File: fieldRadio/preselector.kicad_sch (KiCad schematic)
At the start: 48 parts, among them K1 G5V-2, K2 G5V-2, K3 G5V-2, K4 G5V-2, Q1 MMBT3904, Q2 MMBT3904, Q3 MMBT3904, Q4 MMBT3904, Q5 MMBT3904

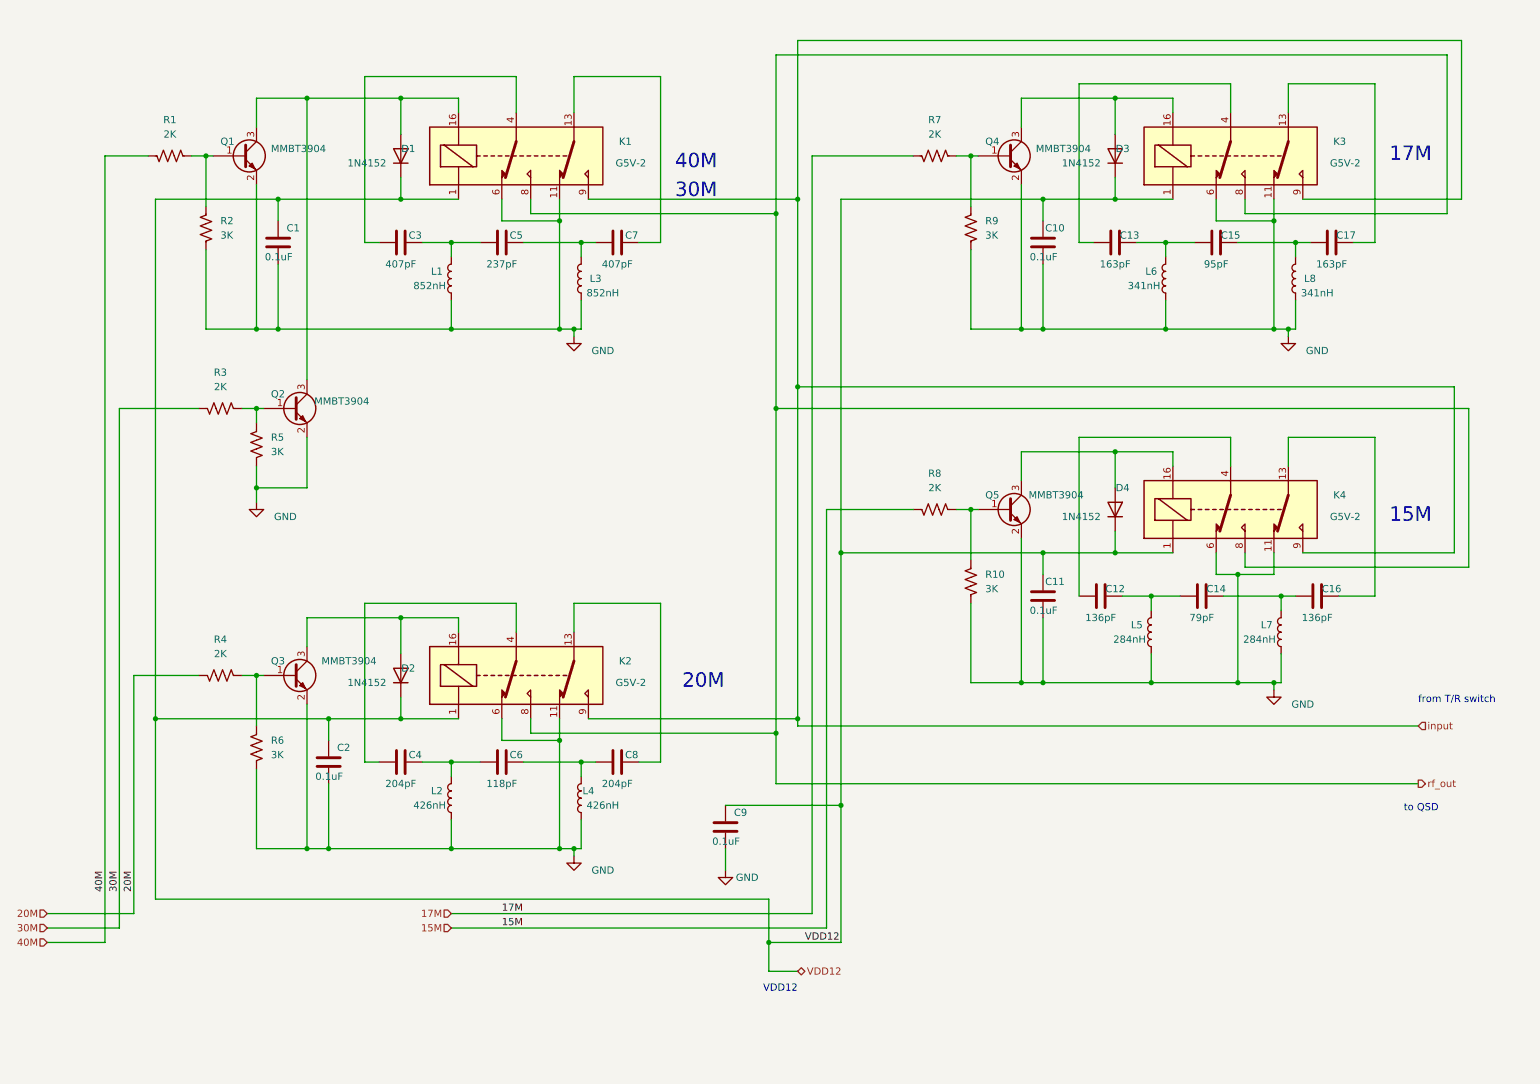
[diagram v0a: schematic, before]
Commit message: Building fieldradio schematic
in process of building field radio schematics
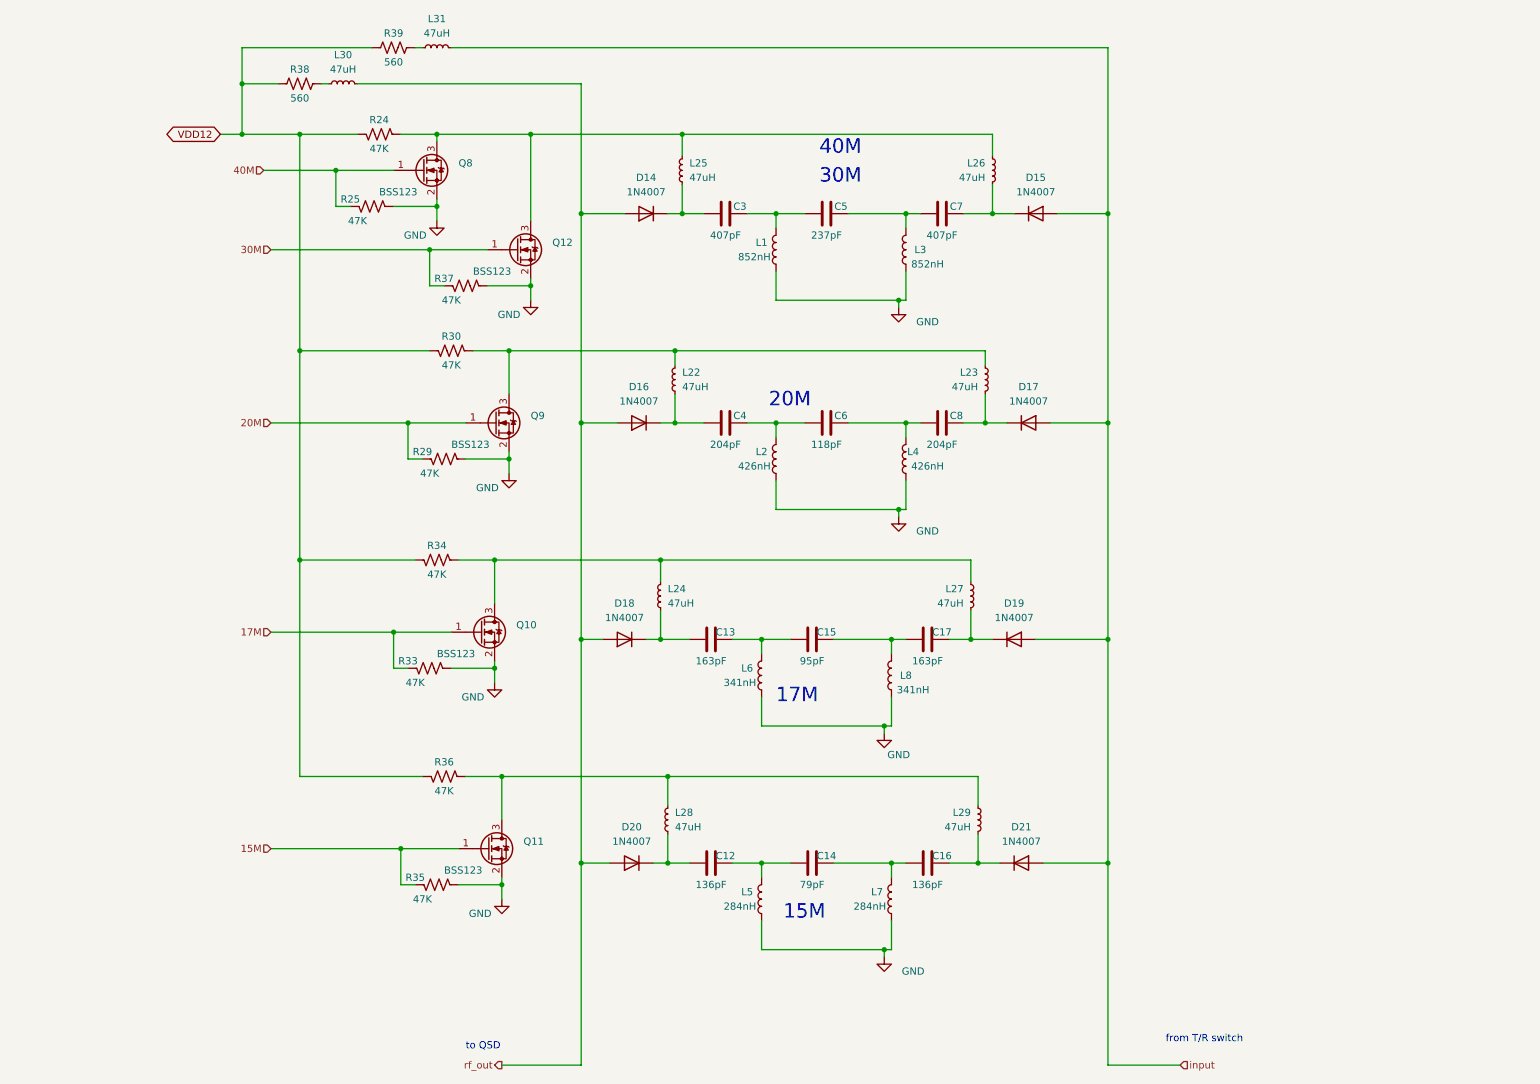
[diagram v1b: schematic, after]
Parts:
- removed C1, C10, C11, C2, C9: 0.1uF, Capacitor_SMD:C_0603_1608Metric_Pad1.08x0.95mm_HandSolder, symbol Device:C
- removed D1, D2, D3, D4: 1N4152, Diode_THT:D_DO-41_SOD81_P7.62mm_Horizontal, symbol Device:D
- removed K1, K2, K3, K4: G5V-2, Relay_THT:Relay_DPDT_Omron_G5V-2, symbol Relay:G5V-2
- removed Q1, Q2, Q3, Q4, Q5: MMBT3904, Package_TO_SOT_SMD:SOT-23, symbol Device:Q_NPN_BEC
- removed R1, R3, R4, R7, R8: 2K, Resistor_SMD:R_0603_1608Metric_Pad0.98x0.95mm_HandSolder, symbol Device:R_US
- removed R10, R2, R5, R6, R9: 3K, Resistor_SMD:R_0603_1608Metric_Pad0.98x0.95mm_HandSolder, symbol Device:R_US
- added D14, D15, D16, D17, D18, D19, D20, D21: 1N4007, Diode_THT:D_DO-41_SOD81_P10.16mm_Horizontal, symbol Diode:1N4007
- added L22, L23, L24, L25, L26, L27, L28, L29, L30, L31: 47uH, Inductor_THT:L_Axial_L11.0mm_D4.5mm_P7.62mm_Vertical_Fastron_MECC, symbol Device:L_Small
- added Q10, Q11, Q12, Q8, Q9: BSS123, Package_TO_SOT_SMD:SOT-23-3, symbol Device:Q_NMOS_GSD
- added R24, R25, R29, R30, R33, R34, R35, R36, R37: 47K, Resistor_SMD:R_0603_1608Metric_Pad0.98x0.95mm_HandSolder, symbol Device:R_US
- added R38, R39: 560, Resistor_THT:R_Axial_DIN0617_L17.0mm_D6.0mm_P20.32mm_Horizontal, symbol Device:R_US
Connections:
- net 15M: now also Q11.1 (G), R35.2
- net 17M: now also Q10.1 (G), R33.2
- net 20M: now also Q9.1 (G), R29.2
- net 30M: now also Q12.1 (G), R37.2
- net 40M: now also Q8.1 (G), R25.2
- net GND: now also Q10.2 (S), Q11.2 (S), Q12.2 (S), Q8.2 (S), Q9.2 (S), R25.1, R29.1, R33.1, R35.1, R37.1
- net VDD12: now also R24.2, R30.2, R34.2, R36.2, R38.1, R39.1
- net input: now also D15.2 (A), D17.2 (A), D19.2 (A), D21.2 (A), L31.2
- net rf_out: now also D14.2 (A), D16.2 (A), D18.2 (A), D20.2 (A), L30.2
- net at C8.1: now also D17.1 (K), L23.1
- net at C4.2: now also D16.1 (K), L22.1
- net at C16.1: now also D21.1 (K), L29.1
- net at C12.2: now also D20.1 (K), L28.1
- net at C17.1: now also D19.1 (K), L27.1
- net at C13.2: now also D18.1 (K), L24.1
- net at C7.1: now also D15.1 (K), L26.1
- net at C3.2: now also D14.1 (K), L25.1
- new net: L31.1, R39.2
- new net: L28.2, L29.2, Q11.3 (D), R36.1
- new net: L24.2, L27.2, Q10.3 (D), R34.1
- new net: L22.2, L23.2, Q9.3 (D), R30.1
- new net: L25.2, L26.2, Q12.3 (D), Q8.3 (D), R24.1
- new net: L30.1, R38.2
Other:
- note removed: "VDD12"
- moved on the sheet: C12, C13, C14, C15, C16, C17, C3, C4, C5, C6, C7, C8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

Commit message: More schematic dev.
More schematic development
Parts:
- removed C5: 237pF, Capacitor_SMD:C_0805_2012Metric_Pad1.18x1.45mm_HandSolder, symbol Device:C
- removed L1: 852nH, Inductor_THT:L_Toroid_Vertical_L13.0mm_W6.5mm_P5.60mm, symbol Device:L
- added C91: 237pF, Capacitor_SMD:C_0805_2012Metric_Pad1.18x1.45mm_HandSolder, symbol Device:C
- added L32: 852nH, Inductor_THT:L_Toroid_Vertical_L13.0mm_W6.5mm_P5.60mm, symbol Device:L
- renumbered C13 to C85, C12 to C86, C3 to C87, C4 to C88, C15 to C89, C14 to C90, C6 to C92, C17 to C93, C16 to C94, C7 to C95, C8 to C96, D18 to D22, D20 to D23, D16 to D24, D14 to D25, D19 to D26, D21 to D27, D17 to D28, D15 to D29, L30 to L24, L31 to L25, L24 to L26, L28 to L27, L22 to L28, L25 to L29, L6 to L30, L5 to L31, L2 to L33, L8 to L34, L7 to L35, L3 to L36, L4 to L37, L27 to L38, L29 to L39, L23 to L40, L26 to L41, Q8 to Q18, Q10 to Q19, Q11 to Q20, Q9 to Q21, Q12 to Q22, R38 to R84, R25 to R85, R24 to R86, R39 to R87, R33 to R88, R34 to R89, R35 to R90, R29 to R91, R36 to R92, R30 to R93, R37 to R94
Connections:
- net GND: now also L32.2
- net at C95.2, L36.1: now also C91.1
- net at C87.1: now also C91.2, L32.1

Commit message: Clean Up
Schematic clean up in prep for layout
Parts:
- L23: renamed from L24; footprint Inductor_THT:L_Axial_L11.0mm_D4.5mm_P7.62mm_Vertical_Fastron_MECC -> Inductor_THT:L_Axial_L13.0mm_D4.5mm_P15.24mm_Horizontal_Fastron_HCCC
- L24: renamed from L25; footprint Inductor_THT:L_Axial_L11.0mm_D4.5mm_P7.62mm_Vertical_Fastron_MECC -> Inductor_THT:L_Axial_L13.0mm_D4.5mm_P15.24mm_Horizontal_Fastron_HCCC
- L25: renamed from L26; footprint Inductor_THT:L_Axial_L11.0mm_D4.5mm_P7.62mm_Vertical_Fastron_MECC -> Inductor_THT:L_Axial_L13.0mm_D4.5mm_P15.24mm_Horizontal_Fastron_HCCC
- L26: renamed from L27; footprint Inductor_THT:L_Axial_L11.0mm_D4.5mm_P7.62mm_Vertical_Fastron_MECC -> Inductor_THT:L_Axial_L13.0mm_D4.5mm_P15.24mm_Horizontal_Fastron_HCCC
- L27: renamed from L28; footprint Inductor_THT:L_Axial_L11.0mm_D4.5mm_P7.62mm_Vertical_Fastron_MECC -> Inductor_THT:L_Axial_L13.0mm_D4.5mm_P15.24mm_Horizontal_Fastron_HCCC
- L28: renamed from L29; footprint Inductor_THT:L_Axial_L11.0mm_D4.5mm_P7.62mm_Vertical_Fastron_MECC -> Inductor_THT:L_Axial_L13.0mm_D4.5mm_P15.24mm_Horizontal_Fastron_HCCC
- L37: renamed from L38; footprint Inductor_THT:L_Axial_L11.0mm_D4.5mm_P7.62mm_Vertical_Fastron_MECC -> Inductor_THT:L_Axial_L13.0mm_D4.5mm_P15.24mm_Horizontal_Fastron_HCCC
- L38: renamed from L39; footprint Inductor_THT:L_Axial_L11.0mm_D4.5mm_P7.62mm_Vertical_Fastron_MECC -> Inductor_THT:L_Axial_L13.0mm_D4.5mm_P15.24mm_Horizontal_Fastron_HCCC
- L39: renamed from L40; footprint Inductor_THT:L_Axial_L11.0mm_D4.5mm_P7.62mm_Vertical_Fastron_MECC -> Inductor_THT:L_Axial_L13.0mm_D4.5mm_P15.24mm_Horizontal_Fastron_HCCC
- L40: renamed from L41; footprint Inductor_THT:L_Axial_L11.0mm_D4.5mm_P7.62mm_Vertical_Fastron_MECC -> Inductor_THT:L_Axial_L13.0mm_D4.5mm_P15.24mm_Horizontal_Fastron_HCCC
- renumbered C92 to C100, C93 to C101, C94 to C102, C95 to C103, C96 to C104, C85 to C93, C86 to C94, C87 to C95, C88 to C96, C89 to C97, C90 to C98, C91 to C99, D22 to D19, D23 to D20, D24 to D21, D25 to D22, D26 to D23, D27 to D24, D28 to D25, D29 to D26, L30 to L29, L31 to L30, L32 to L31, L33 to L32, L34 to L33, L35 to L34, L36 to L35, L37 to L36, Q18 to Q14, Q19 to Q15, Q20 to Q16, Q21 to Q17, Q22 to Q18, R84 to R78, R85 to R79, R86 to R80, R87 to R81, R88 to R82, R89 to R83, R90 to R84, R91 to R85, R92 to R86, R93 to R87, R94 to R88

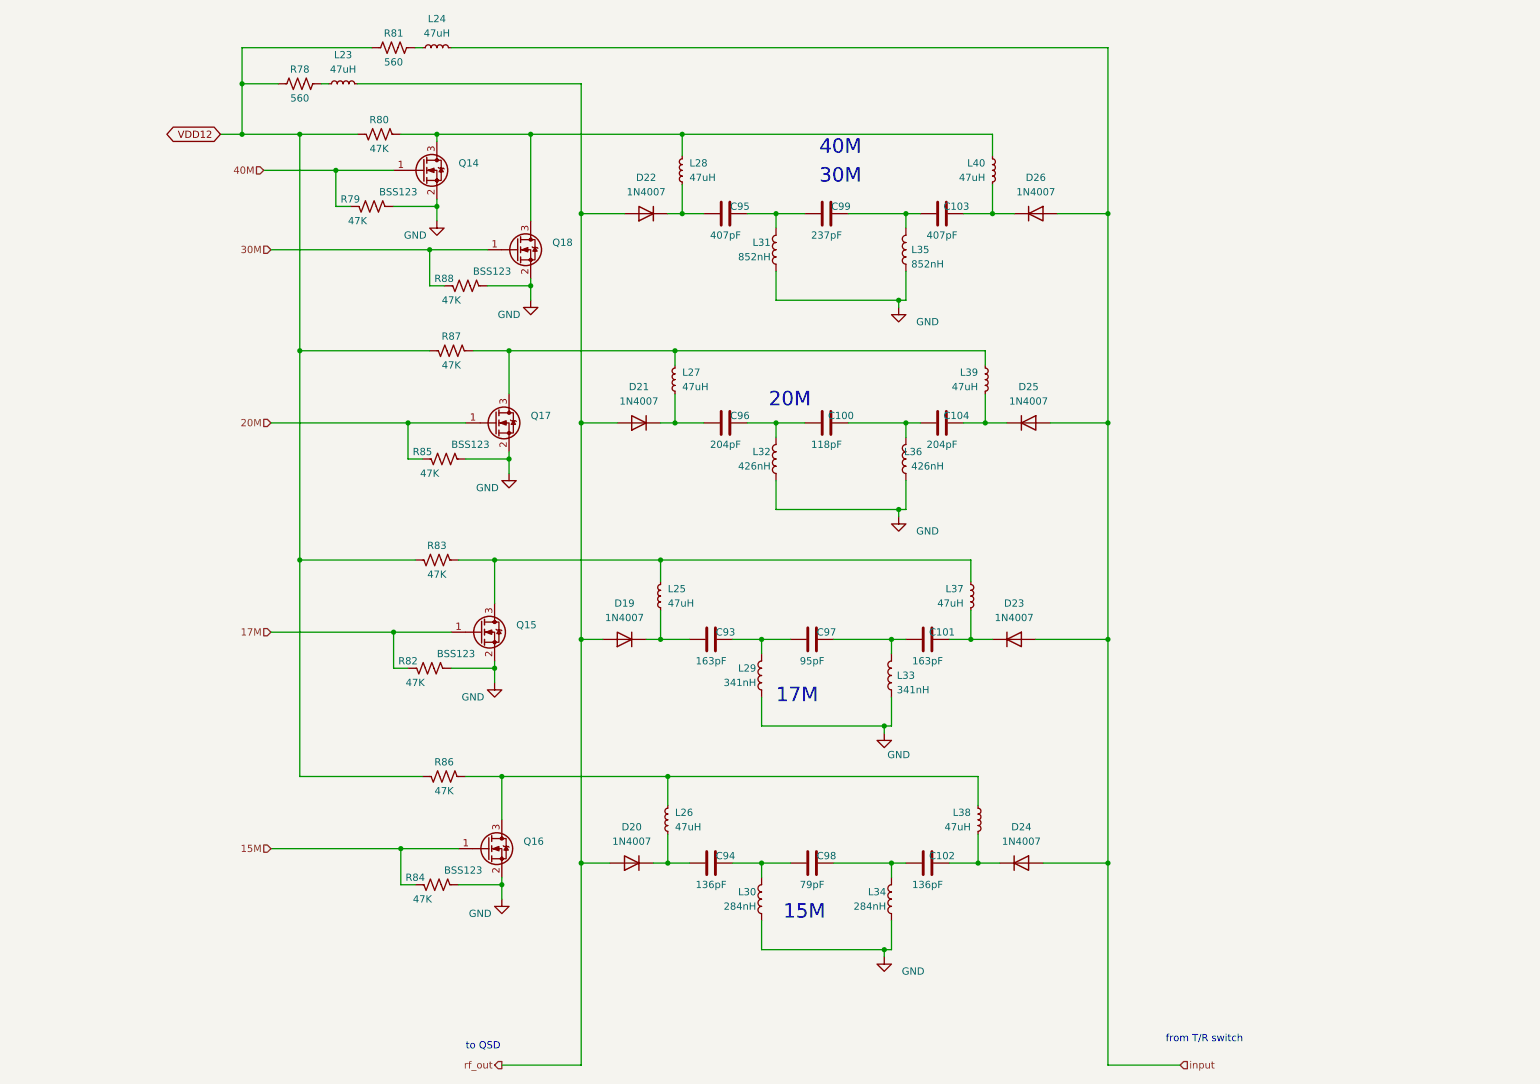
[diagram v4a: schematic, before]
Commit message: Placement of preselector and qsd
Finished placement of these two blocks
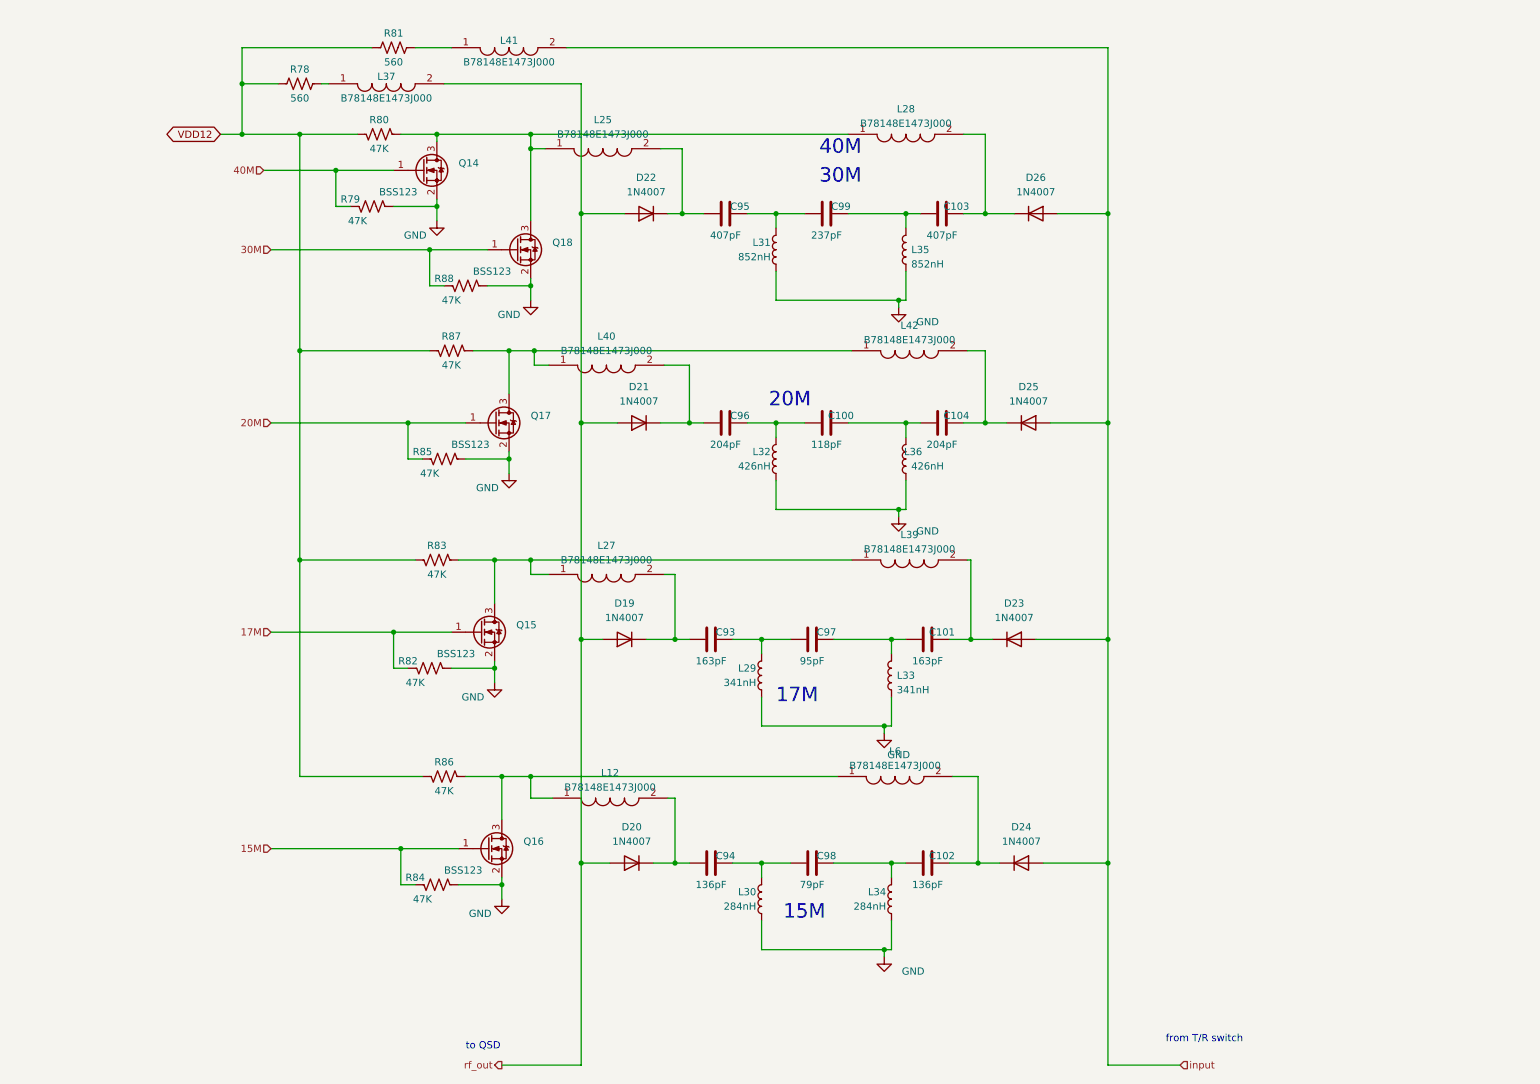
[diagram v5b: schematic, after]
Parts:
- removed L23, L24, L25, L26, L27, L28, L37, L38, L39, L40: 47uH, Inductor_THT:L_Axial_L13.0mm_D4.5mm_P15.24mm_Horizontal_Fastron_HCCC, symbol Device:L_Small
- added L12, L25, L27, L28, L37, L39, L40, L41, L42, L6: B78148E1473J000, B78148E, symbol SamacSys_Parts:B78148E1473J000
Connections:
- net input: now also L41.2
- net rf_out: now also L37.2
- net at R81.2: now also L41.1
- net at Q16.3 (D), R86.1: now also L12.1, L6.1
- net at C94.2, D20.1 (K): now also L12.2
- net at Q15.3 (D), R83.1: now also L27.1, L39.1
- net at C101.1, D23.1 (K): now also L39.2
- net at C96.2, D21.1 (K): now also L40.2
- net at C102.1, D24.1 (K): now also L6.2
- net at Q17.3 (D), R87.1: now also L40.1, L42.1
- net at C104.1, D25.1 (K): now also L42.2
- net at C93.2, D19.1 (K): now also L27.2
- net at C103.1, D26.1 (K): now also L28.2
- net at Q14.3 (D), Q18.3 (D), R80.1: now also L25.1, L28.1
- net at C95.2, D22.1 (K): now also L25.2
- net at R78.2: now also L37.1
